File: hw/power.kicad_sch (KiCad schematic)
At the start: 38 parts, among them J1 TYPE-C-31-M-13C, J2 Conn_01x02, Q1 DMC2400UV, U2 NPM1100-CAAA-R

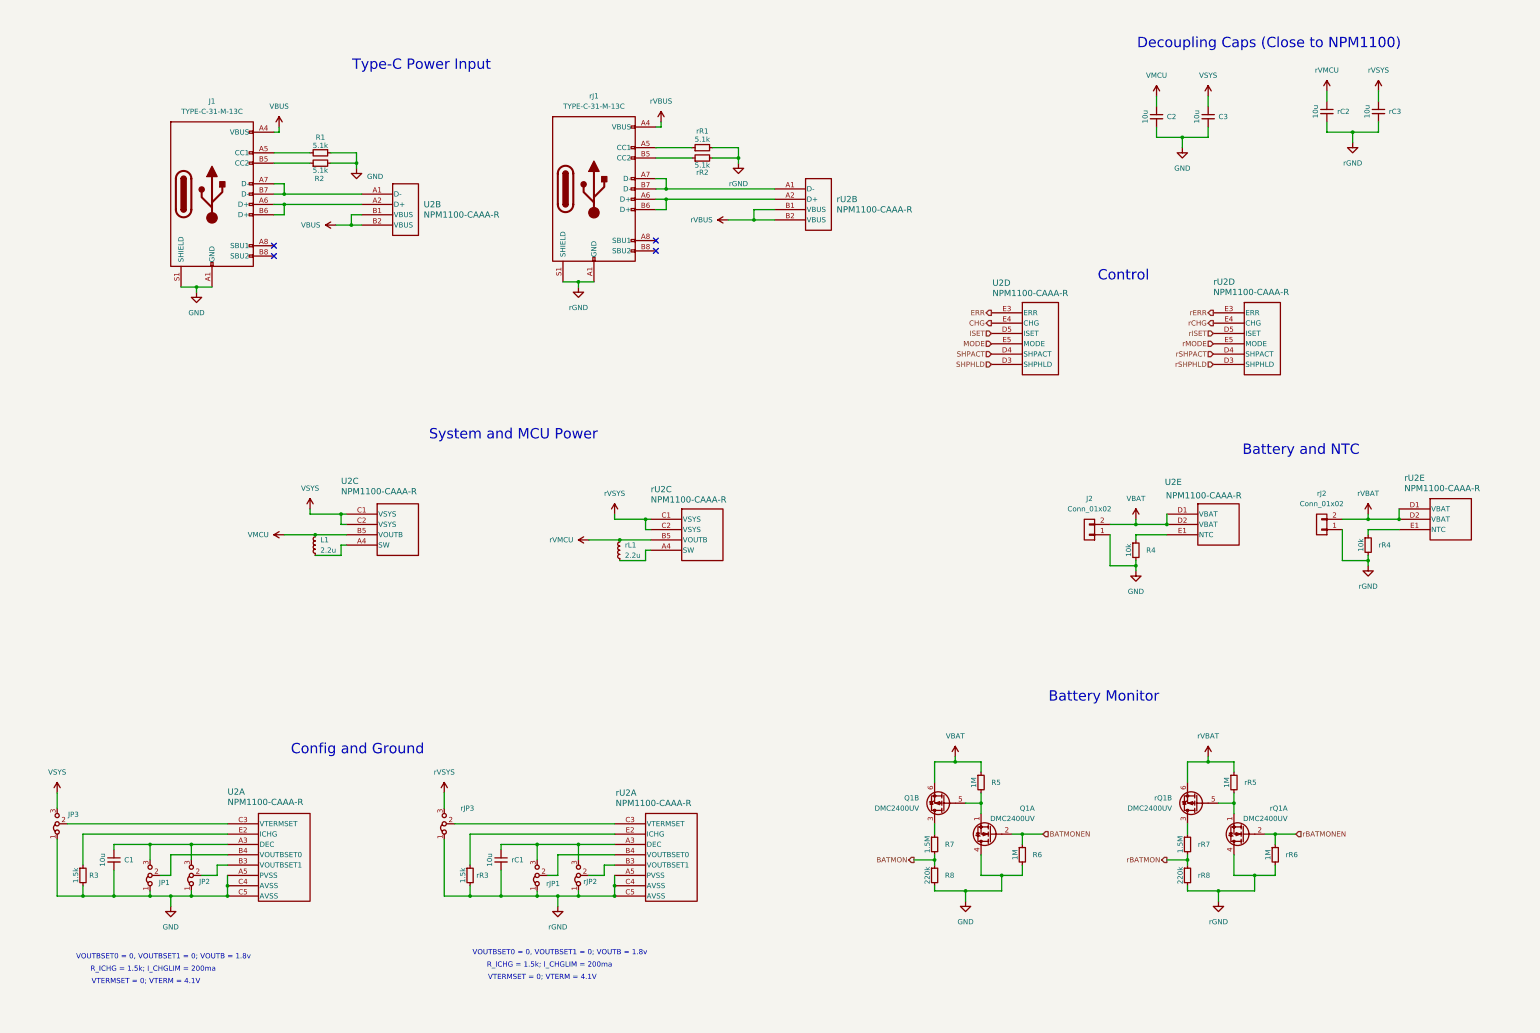
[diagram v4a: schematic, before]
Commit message: Update to NPM1300 for 4 power rails (needed for fpga). NPM1300 still needs decoupling caps
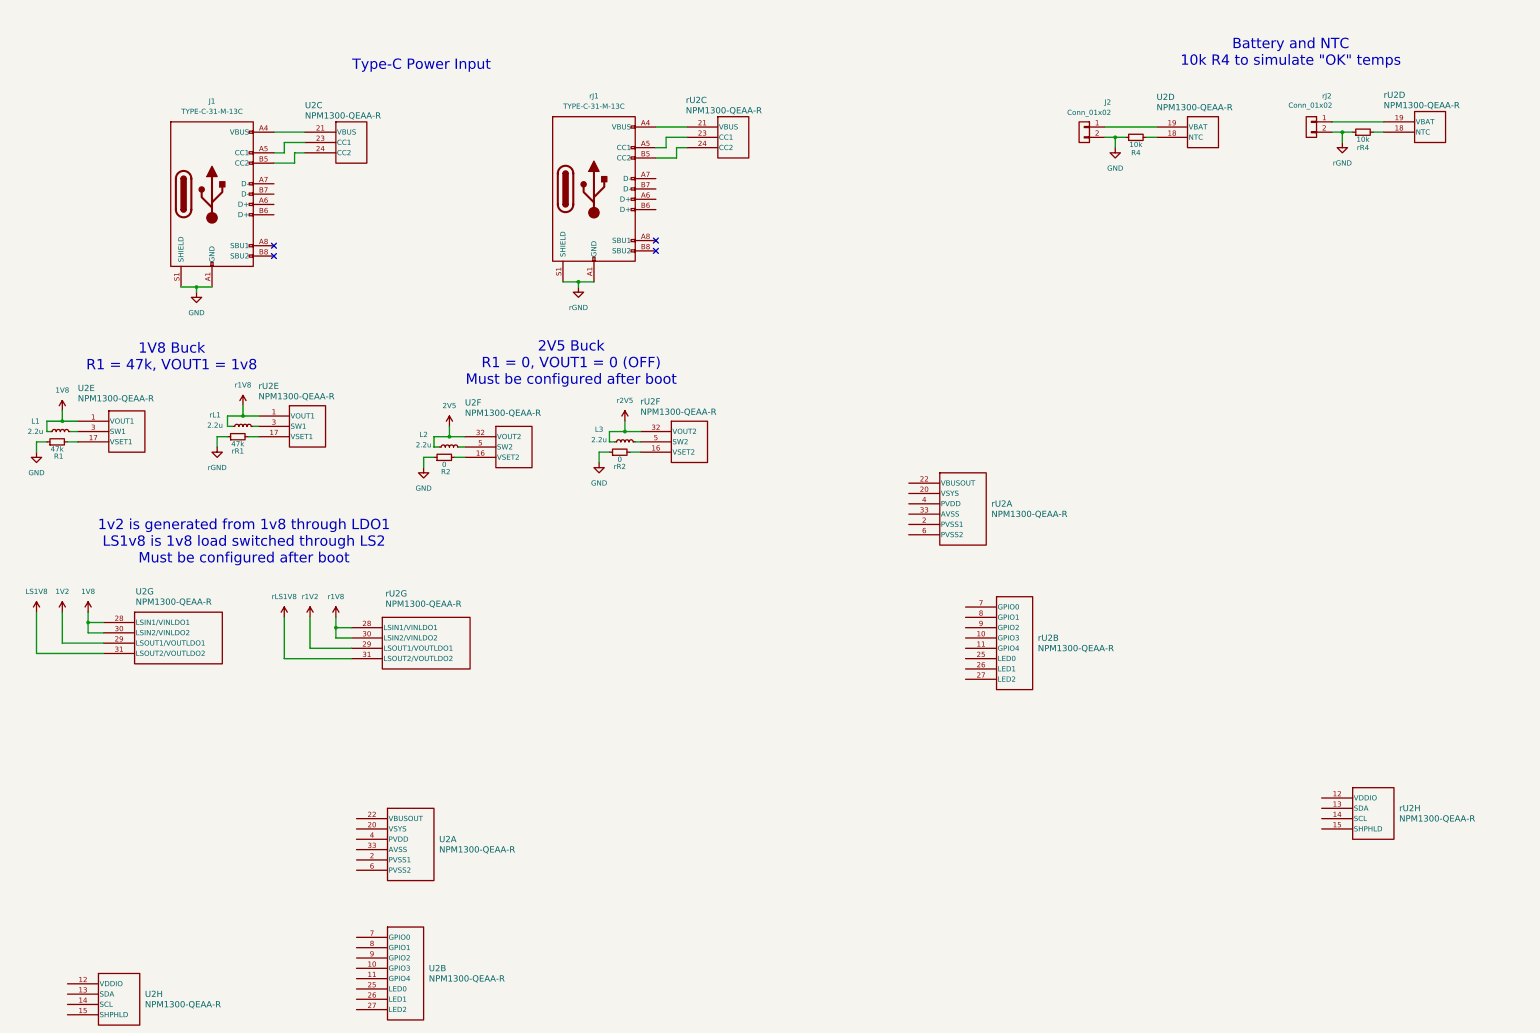
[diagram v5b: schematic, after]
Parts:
- removed C1, C2, C3, rC1, rC2, rC3: 10u, symbol Alidade:C
- removed JP1, JP2, JP3, rJP1, rJP2, rJP3: Jumper_3_Bridged12, symbol Alidade:Jumper_3_Bridged12
- removed Q1, rQ1: DMC2400UV, symbol Alidade:DMC2400UV
- removed R3, rR3: 1.5k, symbol Alidade:R
- removed R5, R6, rR5, rR6: 1M, symbol Alidade:R
- removed R7, rR7: 1.5M, symbol Alidade:R
- removed R8, rR8: 220k, symbol Alidade:R
- removed U2, rU2: NPM1100-CAAA-R, Alidade:WLCSP_2p075X2p075_NOR, symbol Alidade:NPM1100-CAAA-R
- added L2, L3: 2.2u, symbol Alidade:L
- added U2, rU2: NPM1300-QEAA-R, Alidade:QFN32_5X5_NOR, symbol Alidade:NPM1300-QEAA-R
- R1, rR1: value 5.1k -> 47k
- R2, rR2: value 5.1k -> 0
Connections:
- net VBAT is gone; now on net GND: J2.2 (Pin_2)
- net rVBAT is gone; now on net rGND: rJ2.2 (Pin_2)
- net GND: now also R2.1, R4.1, rR2.1; no longer J2.1 (Pin_1), R2.2, R4.2
- net rGND: now also rR1.1, rR4.1; no longer rJ2.1 (Pin_1), rR1.2, rR2.2, rR4.2
- net 1V8: now reaches L1.1
- net 1V8: now also U2.1 (VOUT1), U2.28 (LSIN1/VINLDO1), U2.30 (LSIN2/VINLDO2)
- net at rJ1.B5 (CC2): now also rU2.24 (CC2); no longer rR2.1
- net at rJ1.A5 (CC1): now also rU2.23 (CC1); no longer rR1.1
- net at rJ1.A6 (D+): no longer rJ1.B6 (D+)
- net at rJ1.A7 (D-): no longer rJ1.B7 (D-)
- net r1V8: now reaches rL1.1
- net r1V8: now also rU2.1 (VOUT1), rU2.28 (LSIN1/VINLDO1), rU2.30 (LSIN2/VINLDO2)
- net at J1.B5 (CC2): now also U2.24 (CC2); no longer R2.1
- net at J1.A5 (CC1): now also U2.23 (CC1); no longer R1.2
- net at J1.A6 (D+): no longer J1.B6 (D+)
- net at J1.A7 (D-): no longer J1.B7 (D-)
- net VBUS: no longer names the net of J1.A4 (VBUS), J1.A9 (VBUS), J1.B4 (VBUS), J1.B9 (VBUS)
- net VBUS: now also U2.21 (VBUS)
- net VMCU: no longer names the net of L1.2
- net VMCU: now also U2.3 (SW1)
- net rVBUS: no longer names the net of rJ1.A4 (VBUS), rJ1.A9 (VBUS), rJ1.B4 (VBUS), rJ1.B9 (VBUS)
- net rVBUS: now also rU2.21 (VBUS)
- net rVMCU: no longer names the net of rL1.2
- net rVMCU: now also rU2.3 (SW1)
- new net: R4.2, U2.18 (NTC)
- new net: J2.1 (Pin_1), U2.19 (VBAT)
- new net: L2.2, U2.5 (SW2)
- new net: rR4.2, rU2.18 (NTC)
- new net: rJ2.1 (Pin_1), rU2.19 (VBAT)
- new net: R1.2, U2.17 (VSET1)
- new net: R2.2, U2.16 (VSET2)
- new net: rR1.2, rU2.17 (VSET1)
- new net: L3.2, rU2.5 (SW2)
- new net: rR2.2, rU2.16 (VSET2)
- new net 1V2: U2.29 (LSOUT1/VOUTLDO1)
- new net 2V5: L2.1, U2.32 (VOUT2)
- new net LS1V8: U2.31 (LSOUT2/VOUTLDO2)
- new net r1V2: rU2.29 (LSOUT1/VOUTLDO1)
- new net r2V5: L3.1, rU2.32 (VOUT2)
- new net rLS1V8: rU2.31 (LSOUT2/VOUTLDO2)
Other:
- note added: "1V8 Buck R1 = 47k, VOUT1 = 1v8"
- note added: "1v2 is generated from 1v8 through LDO1 LS1v8 is 1v8 load switched through LS2 Must be configured after boot"
- note added: "2V5 Buck R1 = 0, VOUT1 = 0 (OFF) Must be configured after boot"
- note added: "Battery and NTC 10k R4 to simulate "OK" temps"
- note removed: "Battery Monitor"
- note removed: "Battery and NTC"
- note removed: "Config and Ground"
- note removed: "Control"
- note removed: "Decoupling Caps (Close to NPM1100)"
- note removed: "R_ICHG = 1.5k; I_CHGLIM = 200ma"
- note removed: "System and MCU Power"
- note removed: "VOUTBSET0 = 0, VOUTBSET1 = 0; VOUTB = 1.8v"
- note removed: "VTERMSET = 0; VTERM = 4.1V"
- moved on the sheet: J2, R4, rJ2, rR4

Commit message: Decoupling caps
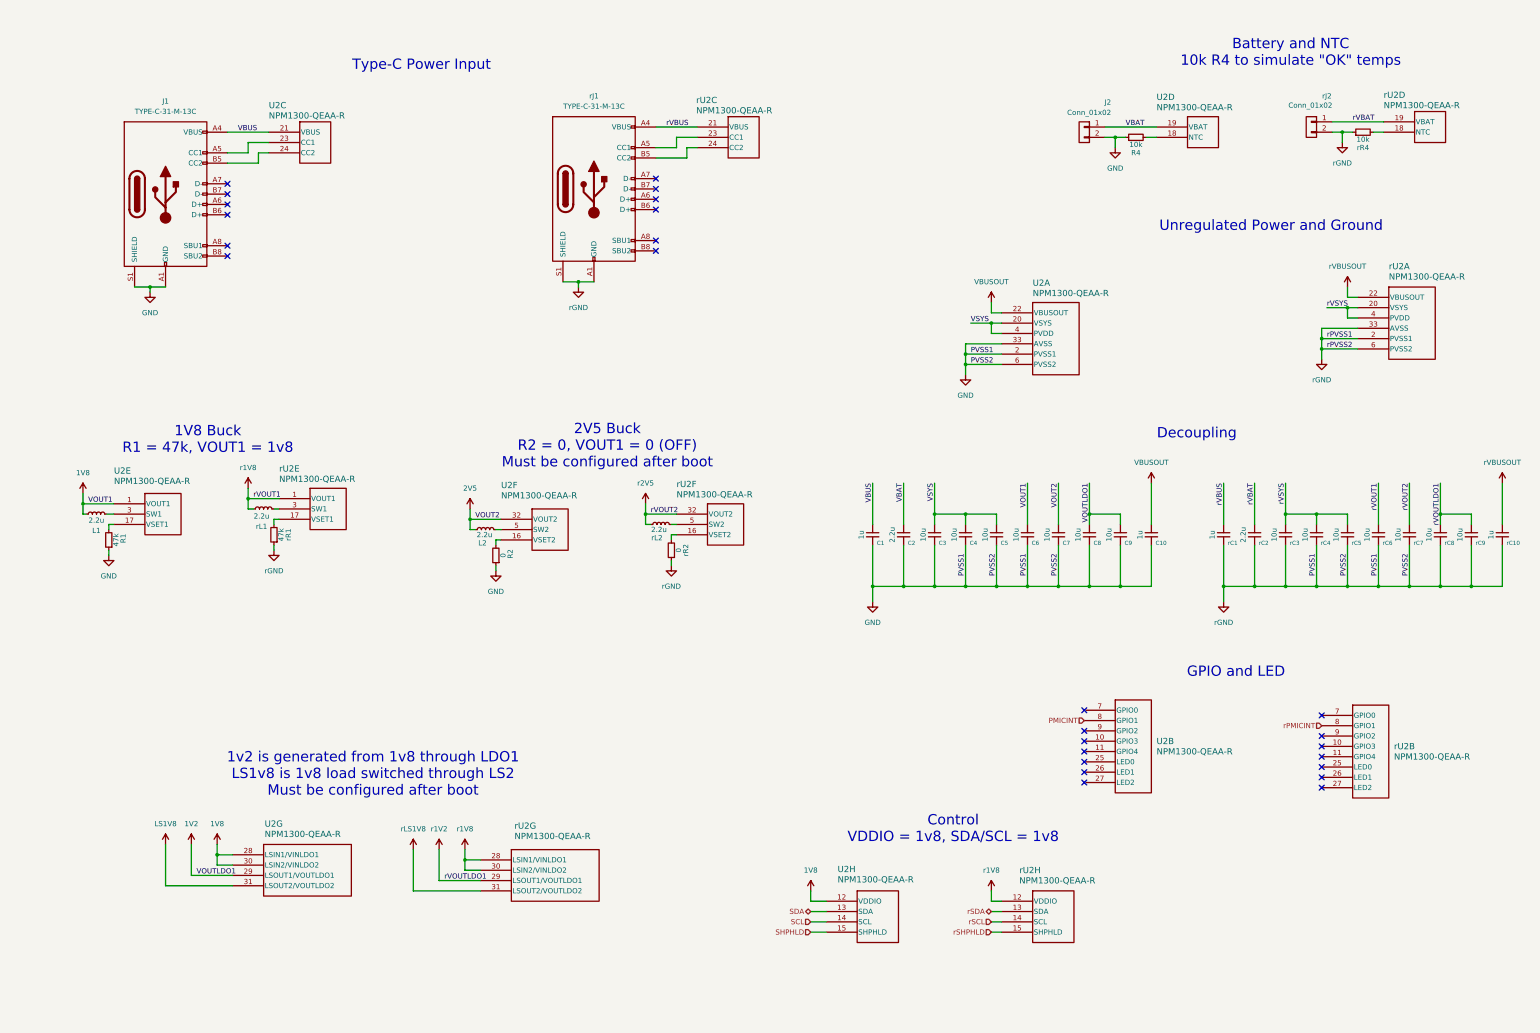
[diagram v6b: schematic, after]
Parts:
- added C1, C10, rC1, rC10: 1u, symbol Alidade:C
- added C2, rC2: 2.2u, symbol Alidade:C
- added C3, C4, C5, C6, C7, C8, C9, rC3, rC4, rC5, rC6, rC7, rC8, rC9: 10u, symbol Alidade:C
- renumbered L3 to rL2
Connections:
- net rGND is gone; now on net GND: rJ1.A1 (GND), rJ1.A12 (GND), rJ1.B1 (GND), rJ1.B12 (GND), rJ1.S1 (SHIELD), rJ2.2 (Pin_2), rR1.1, rR4.1
- net 1V2: now also C8.1, C9.1
- net 1V8: now also U2.12 (VDDIO), C6.1
- net 2V5: now also C7.1
- net GND: now also U2.2 (PVSS1), U2.33 (AVSS), U2.6 (PVSS2), rU2.2 (PVSS1), rU2.33 (AVSS), rU2.6 (PVSS2), C1.2, C10.2, C2.2, C3.2, C4.2, C5.2, C6.2, C7.2, C8.2, C9.2, rC1.2, rC10.2, rC2.2, rC3.2, rC4.2, rC5.2, rC6.2, rC7.2, rC8.2, rC9.2
- net r1V2: now also rC8.1, rC9.1
- net r1V8: now also rU2.12 (VDDIO), rC6.1
- net r2V5: now also rC7.1
- net VSYS: now reaches U2.20 (VSYS)
- net VSYS: now also U2.4 (PVDD), C3.1, C4.1, C5.1
- net VBUSOUT: now reaches U2.22 (VBUSOUT)
- net VBUSOUT: now also C10.1
- net rVBUS: now reaches rJ1.A4 (VBUS), rJ1.A9 (VBUS), rJ1.B4 (VBUS), rJ1.B9 (VBUS), rU2.21 (VBUS)
- net rVBUS: now also rC1.1
- net VBAT: now reaches J2.1 (Pin_1), U2.19 (VBAT)
- net VBAT: now also C2.1
- net rVBAT: now reaches rJ2.1 (Pin_1), rU2.19 (VBAT)
- net rVBAT: now also rC2.1
- net VBUS: now reaches J1.A4 (VBUS), J1.A9 (VBUS), J1.B4 (VBUS), J1.B9 (VBUS), U2.21 (VBUS)
- net VBUS: now also C1.1
- net rSDA: now reaches rU2.13 (SDA)
- net rSCL: now reaches rU2.14 (SCL)
- net rSHPHLD: now reaches rU2.15 (SHPHLD)
- net PMICINT: now reaches U2.8 (GPIO1)
- net rVSYS: now reaches rU2.20 (VSYS)
- net rVSYS: now also rU2.4 (PVDD), rC3.1, rC4.1, rC5.1
- net rVBUSOUT: now reaches rU2.22 (VBUSOUT)
- net rVBUSOUT: now also rC10.1
- net rPMICINT: now reaches rU2.8 (GPIO1)
- net SDA: now reaches U2.13 (SDA)
- net SCL: now reaches U2.14 (SCL)
- net SHPHLD: now reaches U2.15 (SHPHLD)
- no-connect marks 4 -> 26
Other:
- note added: "2V5 Buck R2 = 0, VOUT1 = 0 (OFF) Must be configured after boot"
- note added: "Control VDDIO = 1v8, SDA/SCL = 1v8"
- note added: "Decoupling"
- note added: "GPIO and LED"
- note added: "Unregulated Power and Ground"
- note removed: "2V5 Buck R1 = 0, VOUT1 = 0 (OFF) Must be configured after boot"
- moved on the sheet: J1, L1, L2, R1, R2, U2A, U2B, U2C, U2E, U2F, U2G, U2H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

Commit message: Sheet pins
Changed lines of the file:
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@@
 	)
 	(hierarchical_label "PMICINT"
-		(shape input)
+		(shape output)
 		(at 287.02 194.31 180)
 		(effects
@@
 	)
 	(hierarchical_label "rPMICINT"
-		(shape input)
+		(shape output)
 		(at 345.44 195.58 180)
 		(effects
